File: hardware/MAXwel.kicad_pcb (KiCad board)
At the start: 2 copper layers, 85.1 x 87.8 mm, 155 parts, among them J1 Conn_02x05_Odd_Even, J2 Conn_02x12_Counter_Clockwise, J3 Barrel_Jack_Switch_Pin3Ring, SW1 SW_Push_Dual, SW10 SW_Wuerth_450301014042, SW11 SW_Wuerth_450301014042, SW12 SW_Wuerth_450301014042, SW13 SW_Wuerth_450301014042, SW2 SW_Push_Dual, SW3 SW_Push_Dual, SW4 SW_Push_Dual, SW5 SW_Wuerth_450301014042, SW6 SW_Wuerth_450301014042, SW7 SW_Wuerth_450301014042, SW8 SW_Wuerth_450301014042, SW9 SW_Push_DPDT, U1 D168K, U2 D168K, U3 D168K, U4 D168K, U5 EPM240T100, U6 AMS1117-3.3, X1 50.000, X2 14.756

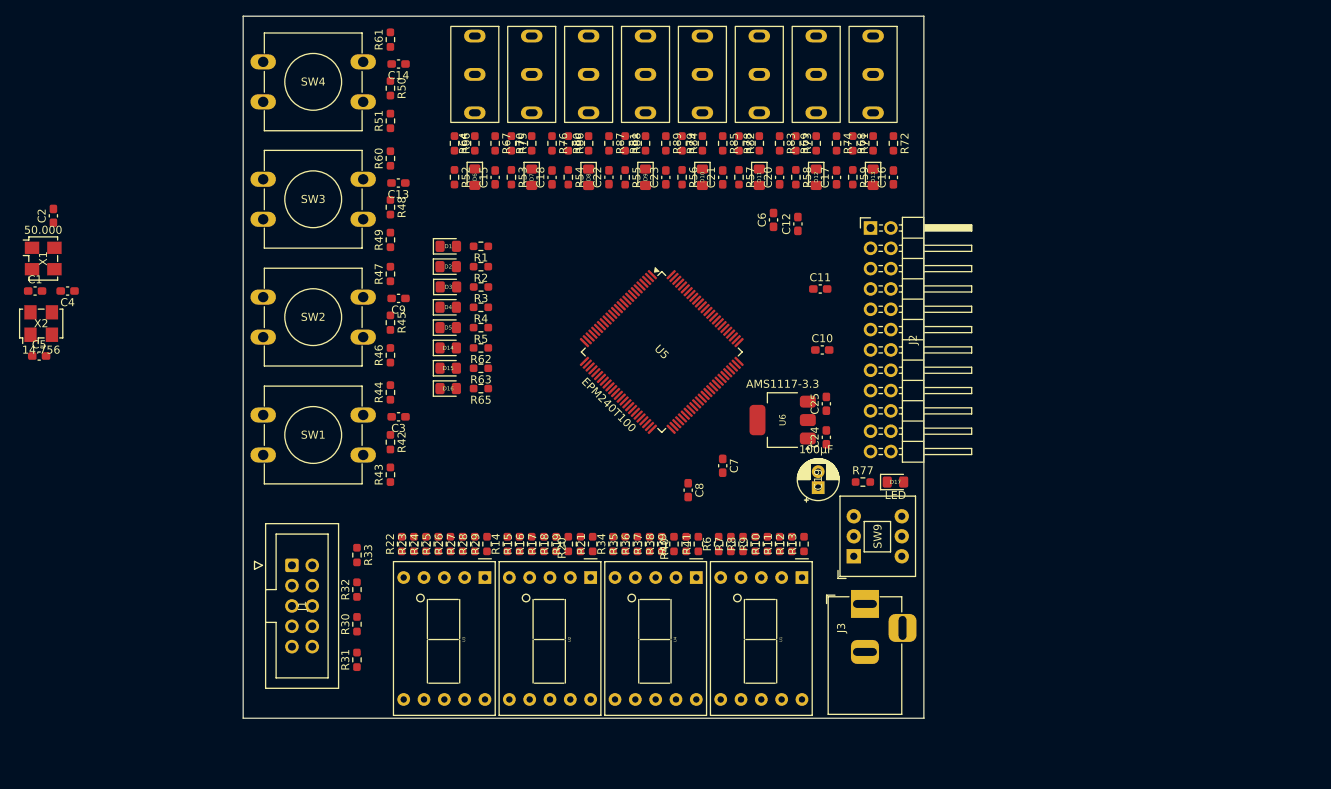
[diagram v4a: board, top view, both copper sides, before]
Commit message: arranged mostly all parts to reduce intersections
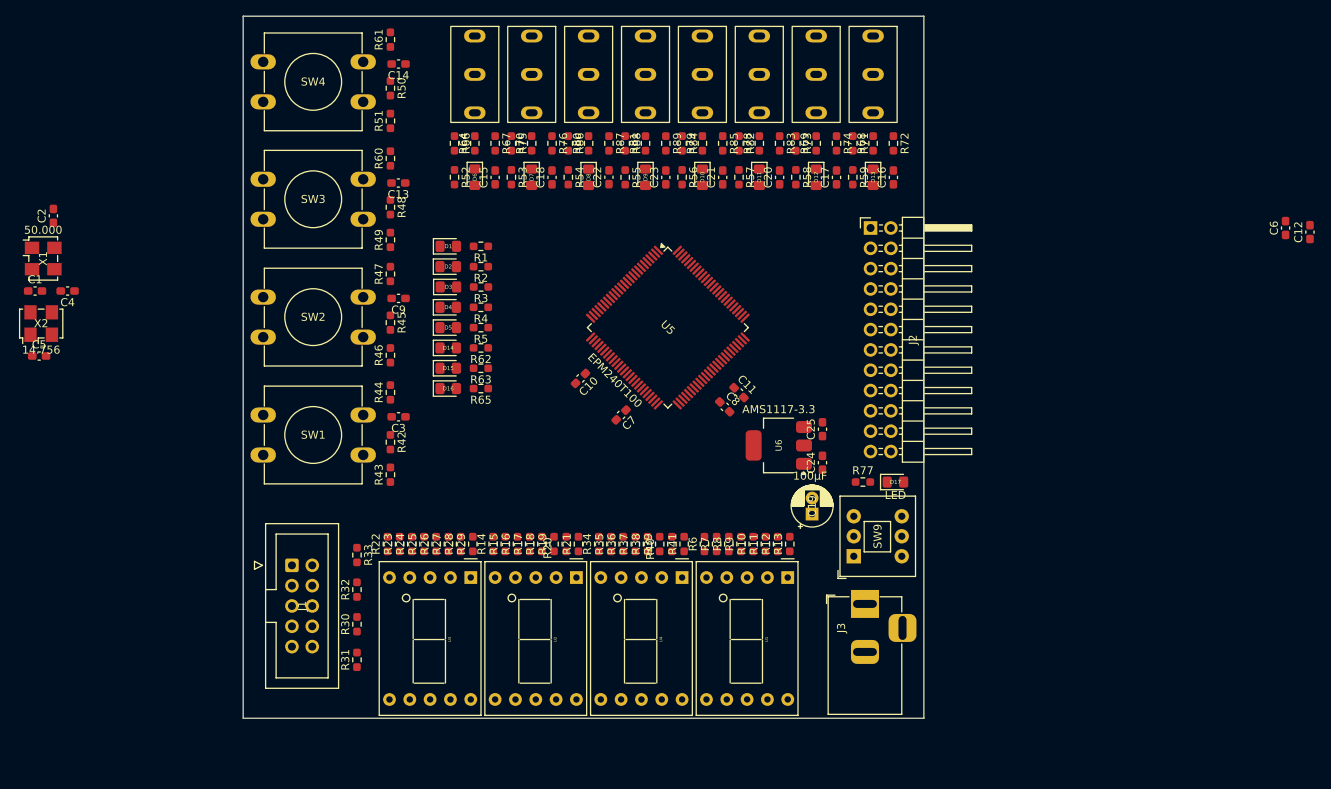
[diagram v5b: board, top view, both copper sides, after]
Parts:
- moved C12 64.0 mm to (237.5, 47.2)
- moved C6 64.0 mm to (234.4, 46.7)
- moved C10 30.4 mm to (146.3, 65.5), turned to -135 degrees
- moved C11 16.5 mm to (166.1, 67.3), turned to -45 degrees
- moved C7 14.2 mm to (151.4, 70.1), turned to -135 degrees
- moved C8 11.4 mm to (164.3, 69.1), turned to -45 degrees
- moved C19 3.39 mm to (175.3, 82.5)
- moved C25 3.21 mm to (176.6, 71.9)
- moved C24 3.21 mm to (176.6, 76.1)
- moved U6 3.21 mm to (171.1, 73.9)
- moved U5 3.14 mm to (157.2, 59.2)
- moved U1 1.78 mm to (172.2, 90.4)
- moved U2 1.78 mm to (145.8, 90.4)
- moved U3 1.78 mm to (132.6, 90.4)
- moved U4 1.78 mm to (159.0, 90.4)
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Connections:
- C15 pad 1: Net-(C15-Pad1) -> Net-(U5-IO1_2)
- C16 pad 1: Net-(C16-Pad1) -> Net-(U5-IO2_86)
- C17 pad 1: Net-(C17-Pad1) -> Net-(U5-IO2_88)
- C18 pad 1: Net-(C18-Pad1) -> Net-(U5-IO2_100)
- C20 pad 1: Net-(C20-Pad1) -> Net-(U5-IO2_90)
- C21 pad 1: Net-(C21-Pad1) -> Net-(U5-IO2_92)
- C22 pad 1: Net-(C22-Pad1) -> Net-(U5-IO2_98)
- C23 pad 1: Net-(C23-Pad1) -> Net-(U5-IO2_96)
- R52 pad 1: unconnected-(R52-Pad1) -> Net-(U5-IO1_3)
- R53 pad 1: unconnected-(R53-Pad1) -> Net-(U5-IO2_1)
- R54 pad 1: unconnected-(R54-Pad1) -> Net-(U5-IO2_99)
- R55 pad 1: unconnected-(R55-Pad1) -> Net-(U5-IO2_97)
- R56 pad 1: unconnected-(R56-Pad1) -> Net-(U5-IO2_95)
- R57 pad 1: unconnected-(R57-Pad1) -> Net-(U5-IO2_91)
- R58 pad 1: unconnected-(R58-Pad1) -> Net-(U5-IO2_89)
- R59 pad 1: unconnected-(R59-Pad1) -> Net-(U5-IO2_87)
- R64 pad 1: Net-(C15-Pad1) -> Net-(U5-IO1_2)
- R68 pad 1: Net-(C16-Pad1) -> Net-(U5-IO2_86)
- R69 pad 1: Net-(C17-Pad1) -> Net-(U5-IO2_88)
- R70 pad 1: Net-(C18-Pad1) -> Net-(U5-IO2_100)
- R78 pad 1: Net-(C20-Pad1) -> Net-(U5-IO2_90)
- R79 pad 1: Net-(C21-Pad1) -> Net-(U5-IO2_92)
- R80 pad 1: Net-(C22-Pad1) -> Net-(U5-IO2_98)
- R81 pad 1: Net-(C23-Pad1) -> Net-(U5-IO2_96)
- U5 pad 1: unconnected-(U5-IO2_1-Pad1) -> Net-(U5-IO2_1)
- U5 pad 100: unconnected-(U5-IO2_100-Pad100) -> Net-(U5-IO2_100)
- U5 pad 2: unconnected-(U5-IO1_2-Pad2) -> Net-(U5-IO1_2)
- U5 pad 3: unconnected-(U5-IO1_3-Pad3) -> Net-(U5-IO1_3)
- U5 pad 52: Bridge_1 -> Bridge_2
- U5 pad 53: Bridge_2 -> Bridge_1
- U5 pad 86: unconnected-(U5-IO2_86-Pad86) -> Net-(U5-IO2_86)
- U5 pad 87: unconnected-(U5-IO2_87-Pad87) -> Net-(U5-IO2_87)
- U5 pad 88: unconnected-(U5-IO2_88-Pad88) -> Net-(U5-IO2_88)
- U5 pad 89: unconnected-(U5-IO2_89-Pad89) -> Net-(U5-IO2_89)
- U5 pad 90: unconnected-(U5-IO2_90-Pad90) -> Net-(U5-IO2_90)
- U5 pad 91: unconnected-(U5-IO2_91-Pad91) -> Net-(U5-IO2_91)
- U5 pad 92: unconnected-(U5-IO2_92-Pad92) -> Net-(U5-IO2_92)
- U5 pad 95: unconnected-(U5-IO2_95-Pad95) -> Net-(U5-IO2_95)
- U5 pad 96: unconnected-(U5-IO2_96-Pad96) -> Net-(U5-IO2_96)
- U5 pad 97: unconnected-(U5-IO2_97-Pad97) -> Net-(U5-IO2_97)
- U5 pad 98: unconnected-(U5-IO2_98-Pad98) -> Net-(U5-IO2_98)
- U5 pad 99: unconnected-(U5-IO2_99-Pad99) -> Net-(U5-IO2_99)

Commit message: switches: R and C placement optimized
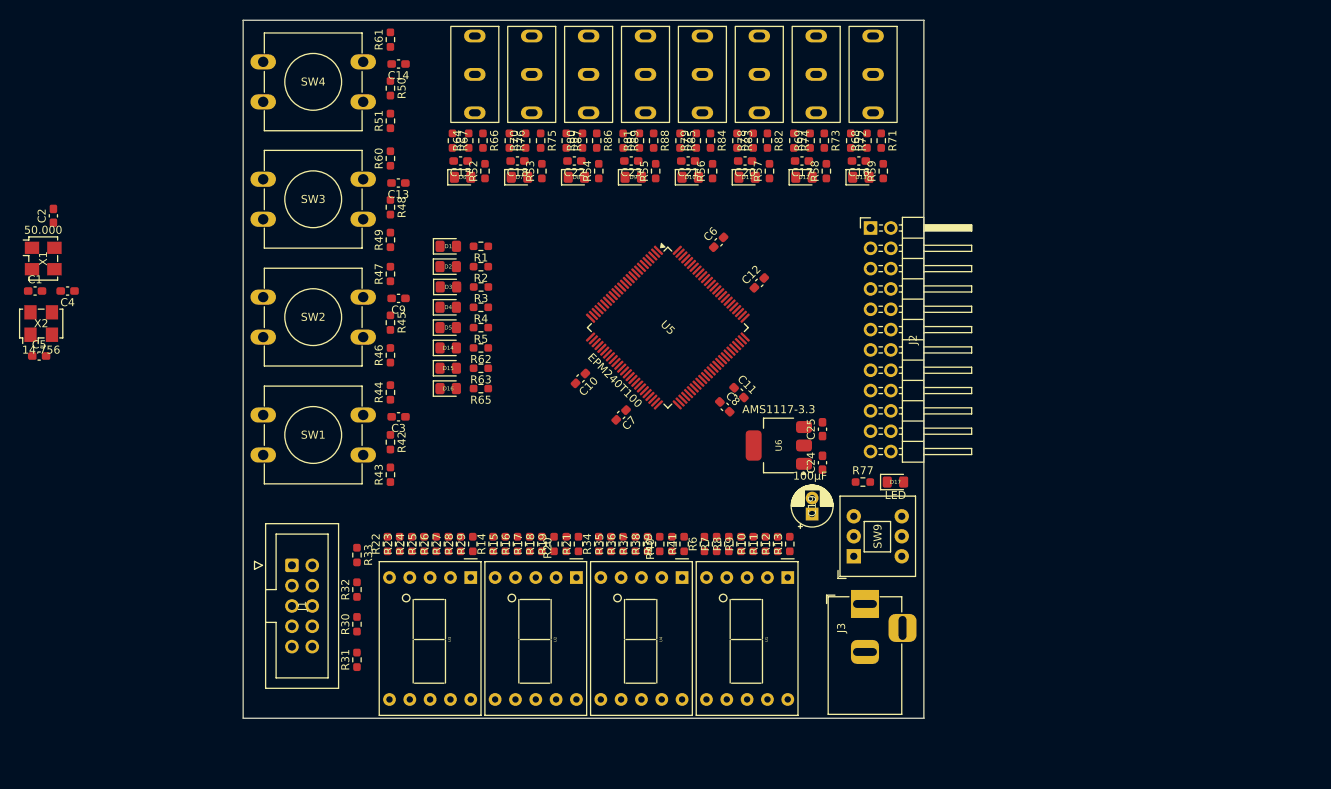
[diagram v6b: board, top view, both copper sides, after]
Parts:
- moved C6 70.9 mm to (163.6, 48.5), turned to 45 degrees
- moved C12 69.1 mm to (168.7, 53.6), turned to 45 degrees
- moved R67 5.34 mm to (130.3, 35.8)
- moved R74 5.34 mm to (173.0, 35.8)
- moved R76 5.34 mm to (137.4, 35.8)
- moved R83 5.34 mm to (165.9, 35.8)
- moved R85 5.34 mm to (158.8, 35.8)
- moved R87 5.34 mm to (144.5, 35.8)
- moved R89 5.34 mm to (151.6, 35.8)
- moved R72 5.34 mm to (180.1, 35.8)
- moved C20 4.78 mm to (166.9, 38.4), turned to 180 degrees
- moved C21 4.78 mm to (159.8, 38.4), turned to 180 degrees
- moved C23 4.78 mm to (152.7, 38.4), turned to 180 degrees
- moved C15 4.78 mm to (131.3, 38.4), turned to 180 degrees
- moved C16 4.78 mm to (181.1, 38.4), turned to 180 degrees
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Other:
- board size 85.1 x 87.8 mm -> 85.1 x 87.2 mm

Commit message: 3/4 of components routed on single layer
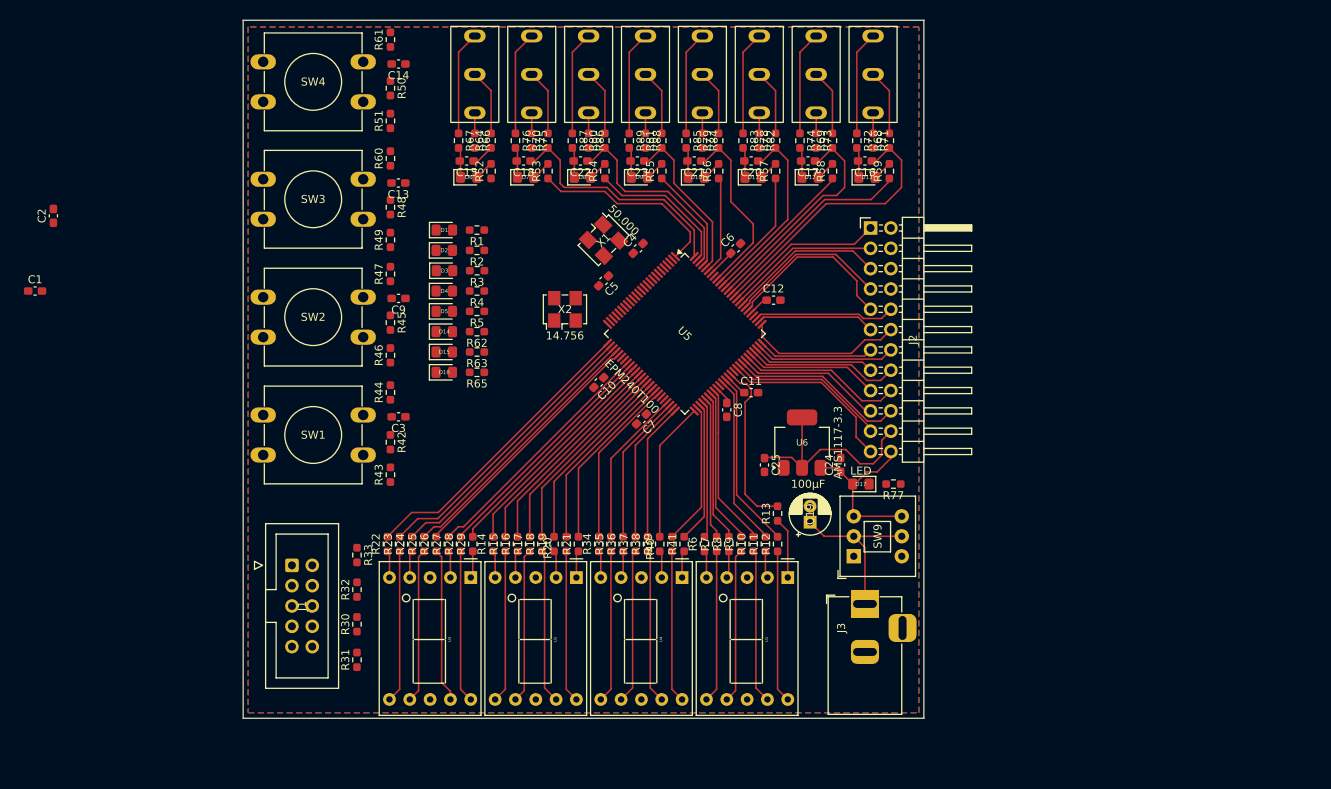
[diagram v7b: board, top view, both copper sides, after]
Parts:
- moved C4 71.5 mm to (153.5, 49.3), turned to 45 degrees
- moved C5 71.2 mm to (149.2, 53.3), turned to -135 degrees
- moved X1 70.1 mm to (149.2, 48.3), turned to -135 degrees
- moved X2 65.5 mm to (144.4, 56.9)
- moved C25 8.52 mm to (169.3, 76.4), turned to -90 degrees
- moved D17 4.33 mm to (181.4, 78.7), turned to 180 degrees
- moved R13 4.11 mm to (170.9, 82.4)
- moved R77 3.82 mm to (185.4, 78.7), turned to 180 degrees
- moved U6 2.93 mm to (174.0, 73.6), turned to 90 degrees
- moved C12 2.80 mm to (170.4, 55.8), turned to 0 degrees
- moved R68 2.79 mm to (184.9, 35.8)
- moved R69 2.79 mm to (177.8, 35.8)
- moved R70 2.79 mm to (142.2, 35.8)
- moved R80 2.79 mm to (149.4, 35.8)
- moved R81 2.79 mm to (156.5, 35.8)
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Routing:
- net +3V3: track 0.00 -> 38.5 mm
- net Net-(U5-IO1_26): track 0.00 -> 37.5 mm
- net Net-(U5-IO1_27): track 0.00 -> 36.2 mm
- net Net-(U5-IO2_86): track 0.00 -> 35.0 mm
- net Net-(U5-IO1_28): track 0.00 -> 34.9 mm
- net Net-(U5-IO1_29): track 0.00 -> 33.6 mm
- net Net-(U5-IO1_30): track 0.00 -> 32.4 mm
- net Net-(U5-IO1_33): track 0.00 -> 31.4 mm
- net Net-(U5-IO2_100): track 0.00 -> 30.4 mm
- net Net-(U5-IO1_34): track 0.00 -> 30.2 mm
- net GND: track 0.00 -> 30.1 mm
- net Net-(U5-IO1_35): track 0.00 -> 29.3 mm
- net Net-(U5-IO2_88): track 0.00 -> 28.3 mm
- net Net-(U5-IO1_36): track 0.00 -> 28.1 mm
- net Net-(U5-IO1_37): track 0.00 -> 27.2 mm
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- added copper zone on B.Cu, net GND
- added copper zone on F.Cu, net GND

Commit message: shifted everything 1 pin to the side for better power routing
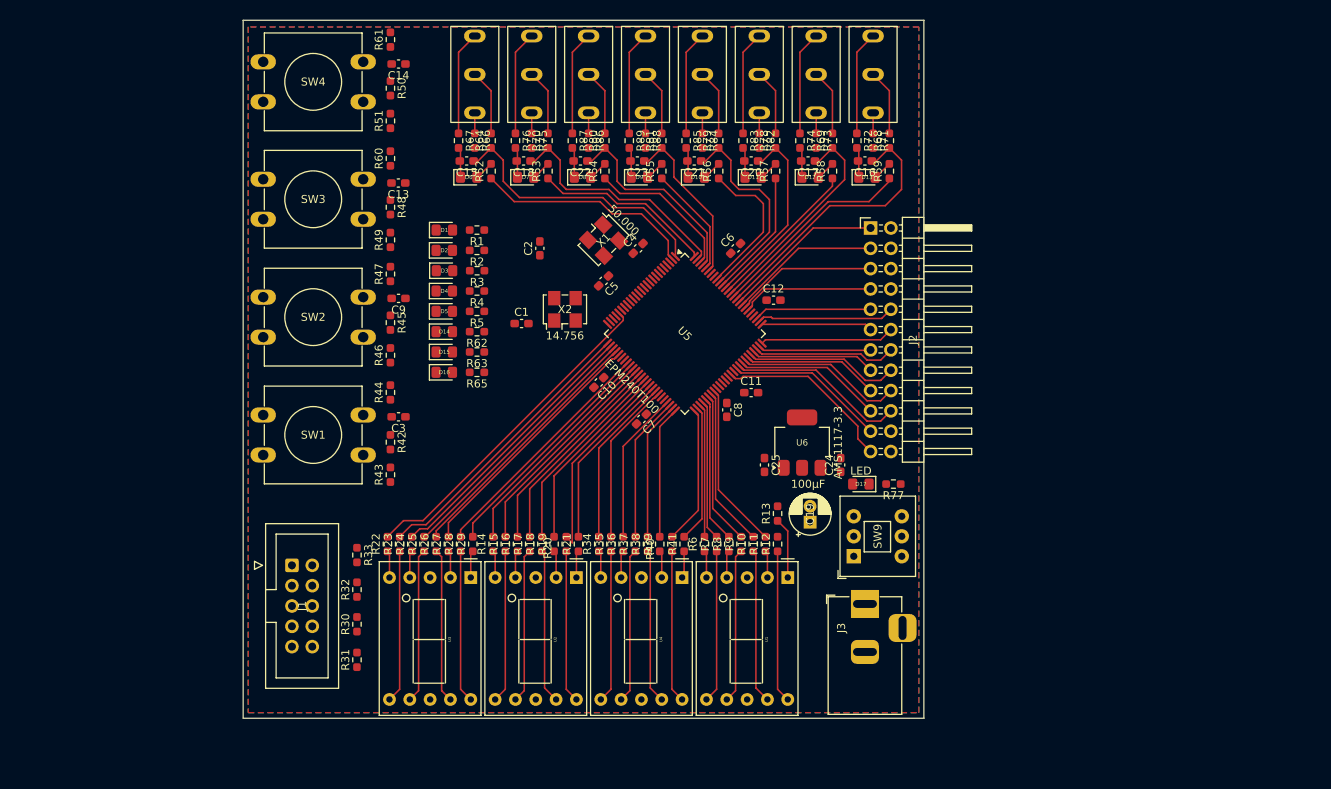
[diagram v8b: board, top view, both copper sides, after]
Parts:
- moved C1 60.9 mm to (138.9, 58.7)
- moved C2 60.9 mm to (141.2, 49.3)
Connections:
- C15 pad 1: Net-(U5-IO1_2) -> Net-(U5-IO2_1)
- C16 pad 1: Net-(U5-IO2_86) -> Net-(U5-IO2_85)
- C17 pad 1: Net-(U5-IO2_88) -> Net-(U5-IO2_87)
- C18 pad 1: Net-(U5-IO2_100) -> Net-(U5-IO2_99)
- C20 pad 1: Net-(U5-IO2_90) -> Net-(U5-IO2_89)
- C21 pad 1: Net-(U5-IO2_92) -> Net-(U5-IO2_91)
- C22 pad 1: Net-(U5-IO2_98) -> Net-(U5-IO2_97)
- C23 pad 1: Net-(U5-IO2_96) -> Net-(U5-IO2_95)
- D7 pad 2: Net-(D7-A) -> unconnected-(D7-A-Pad2)
- R10 pad 2: Net-(U5-IO2_58) -> Net-(U5-IO2_57)
- R11 pad 2: Net-(U5-IO2_61) -> Net-(U5-IO2_58)
- R12 pad 2: Net-(U5-IO2_62/GCLK2) -> Net-(U5-IO2_61)
- R13 pad 2: Net-(U5-IO2_64/GCLK3) -> Net-(U5-IO2_62/GCLK2)
- R14 pad 2: Net-(U5-IO1_36) -> Net-(U5-IO1_35)
- R15 pad 2: Net-(U5-IO1_37) -> Net-(U5-IO1_36)
- R16 pad 2: Net-(U5-IO1_38) -> Net-(U5-IO1_37)
- R17 pad 2: Net-(U5-IO1_39) -> Net-(U5-IO1_38)
- R18 pad 2: Net-(U5-IO1_40) -> Net-(U5-IO1_39)
- R19 pad 2: Net-(U5-IO1_41) -> Net-(U5-IO1_40)
- R20 pad 2: Net-(U5-IO1_42) -> Net-(U5-IO1_41)
- R21 pad 2: Net-(U5-IO1_43/DEV_OE) -> Net-(U5-IO1_42)
- R22 pad 2: Net-(U5-IO1_26) -> Net-(U5-IO1_21)
- R23 pad 2: Net-(U5-IO1_27) -> Net-(U5-IO1_26)
- R24 pad 2: Net-(U5-IO1_28) -> Net-(U5-IO1_27)
- R25 pad 2: Net-(U5-IO1_29) -> Net-(U5-IO1_28)
- R26 pad 2: Net-(U5-IO1_30) -> Net-(U5-IO1_29)
- R27 pad 2: Net-(U5-IO1_33) -> Net-(U5-IO1_30)
- R28 pad 2: Net-(U5-IO1_34) -> Net-(U5-IO1_33)
- R29 pad 2: Net-(U5-IO1_35) -> Net-(U5-IO1_34)
- R34 pad 2: Net-(U5-IO1_44/DEV_CLRn) -> Net-(U5-IO1_43/DEV_OE)
- R35 pad 2: Net-(U5-IO1_47) -> Net-(U5-IO1_44/DEV_CLRn)
- R36 pad 2: Net-(U5-IO1_48) -> Net-(U5-IO1_47)
- R37 pad 2: Net-(U5-IO1_49) -> Net-(U5-IO1_48)
- R38 pad 2: Net-(U5-IO1_50) -> Net-(U5-IO1_49)
- R39 pad 2: Net-(U5-IO1_51) -> Net-(U5-IO1_50)
- R40 pad 2: Bridge_2 -> Net-(U5-IO1_51)
- R52 pad 1: Net-(U5-IO1_3) -> Net-(U5-IO1_2)
- R53 pad 1: Net-(U5-IO2_1) -> Net-(U5-IO2_100)
- R53 pad 2: Net-(D7-A) -> unconnected-(R53-Pad2)
- R54 pad 1: Net-(U5-IO2_99) -> Net-(U5-IO2_98)
- R55 pad 1: Net-(U5-IO2_97) -> Net-(U5-IO2_96)
- R56 pad 1: Net-(U5-IO2_95) -> Net-(U5-IO2_92)
- R57 pad 1: Net-(U5-IO2_91) -> Net-(U5-IO2_90)
- R58 pad 1: Net-(U5-IO2_89) -> Net-(U5-IO2_88)
- R59 pad 1: Net-(U5-IO2_87) -> Net-(U5-IO2_86)
- R6 pad 2: Net-(U5-IO2_54) -> Net-(U5-IO2_53)
- R64 pad 1: Net-(U5-IO1_2) -> Net-(U5-IO2_1)
- R68 pad 1: Net-(U5-IO2_86) -> Net-(U5-IO2_85)
- R69 pad 1: Net-(U5-IO2_88) -> Net-(U5-IO2_87)
- R7 pad 2: Net-(U5-IO2_55) -> Net-(U5-IO2_54)
- R70 pad 1: Net-(U5-IO2_100) -> Net-(U5-IO2_99)
- R78 pad 1: Net-(U5-IO2_90) -> Net-(U5-IO2_89)
- R79 pad 1: Net-(U5-IO2_92) -> Net-(U5-IO2_91)
- R8 pad 2: Net-(U5-IO2_56) -> Net-(U5-IO2_55)
- R80 pad 1: Net-(U5-IO2_98) -> Net-(U5-IO2_97)
- R81 pad 1: Net-(U5-IO2_96) -> Net-(U5-IO2_95)
- R9 pad 2: Net-(U5-IO2_57) -> Net-(U5-IO2_56)
- U5 pad 21: unconnected-(U5-IO1_21-Pad21) -> Net-(U5-IO1_21)
- U5 pad 3: Net-(U5-IO1_3) -> unconnected-(U5-IO1_3-Pad3)
- U5 pad 52: Bridge_2 -> Bridge_1
- U5 pad 53: Bridge_1 -> Net-(U5-IO2_53)
- U5 pad 64: Net-(U5-IO2_64/GCLK3) -> Net-(J2-Pin_23)
- U5 pad 66: Net-(J2-Pin_23) -> Net-(J2-Pin_21)
- U5 pad 67: Net-(J2-Pin_21) -> Net-(J2-Pin_20)
- U5 pad 68: Net-(J2-Pin_20) -> Net-(J2-Pin_19)
- U5 pad 69: Net-(J2-Pin_19) -> Net-(J2-Pin_18)
- U5 pad 70: Net-(J2-Pin_18) -> Net-(J2-Pin_17)
- U5 pad 71: Net-(J2-Pin_17) -> Net-(J2-Pin_16)
- U5 pad 72: Net-(J2-Pin_16) -> Net-(J2-Pin_15)
- U5 pad 73: Net-(J2-Pin_15) -> Net-(J2-Pin_14)
- U5 pad 74: Net-(J2-Pin_14) -> Net-(J2-Pin_13)
- U5 pad 75: Net-(J2-Pin_13) -> Net-(J2-Pin_12)
- U5 pad 76: Net-(J2-Pin_12) -> Net-(J2-Pin_11)
- U5 pad 77: Net-(J2-Pin_11) -> Net-(J2-Pin_10)
- U5 pad 78: Net-(J2-Pin_10) -> Net-(J2-Pin_9)
- U5 pad 81: Net-(J2-Pin_9) -> Net-(J2-Pin_7)
- U5 pad 82: Net-(J2-Pin_7) -> Net-(J2-Pin_5)
- U5 pad 83: Net-(J2-Pin_5) -> Net-(J2-Pin_3)
- U5 pad 84: Net-(J2-Pin_3) -> Net-(J2-Pin_1)
- U5 pad 85: Net-(J2-Pin_1) -> Net-(U5-IO2_85)
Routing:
- net Net-(U5-IO1_21): track 0.00 -> 41.8 mm
- net +3V3: track 38.5 -> 0.00 mm
- net Net-(U5-IO2_85): track 0.00 -> 34.9 mm
- net Net-(U5-IO1_2): track 2.86 -> 27.9 mm
- net Net-(U5-IO2_62/GCLK2): track 22.3 -> 0.00 mm
- net +5V: track 21.9 -> 0.00 mm
- net Net-(U5-IO2_61): track 21.5 -> 0.00 mm
- net Net-(U5-IO2_64/GCLK3): track 21.5 -> 0.00 mm
- net Net-(C19-Pad1): track 21.2 -> 0.00 mm
- net Bridge_2: track 17.8 -> 0.00 mm
- net Net-(U5-IO2_53): track 0.00 -> 16.7 mm
- net Net-(U5-IO2_97): track 13.4 -> 25.8 mm
- net Net-(U5-IO2_99): track 18.5 -> 30.3 mm
- net Net-(U5-IO2_91): track 15.8 -> 26.3 mm
- net Net-(U5-IO2_1): track 24.4 -> 34.3 mm
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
